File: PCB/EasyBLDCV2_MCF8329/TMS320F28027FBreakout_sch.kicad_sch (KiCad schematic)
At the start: 20 parts, among them J2 FTSH-105-01-F-DV-P-TR, U2 TMS320F28027FPTT

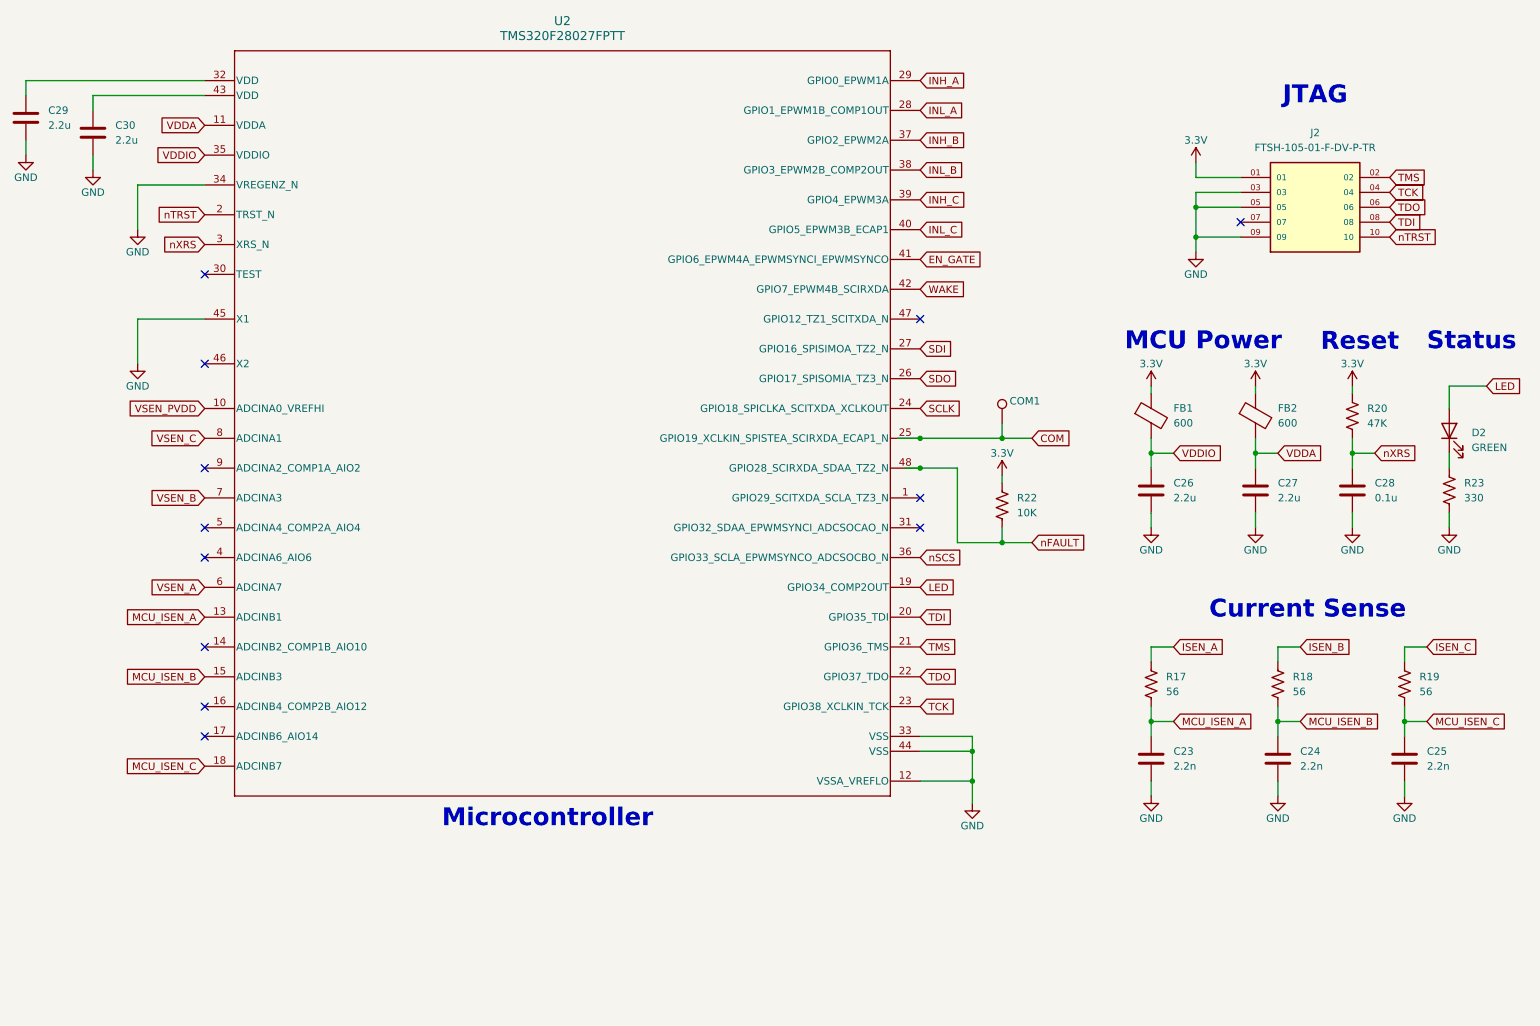
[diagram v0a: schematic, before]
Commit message: Deleted V1 Relics, redid power stage
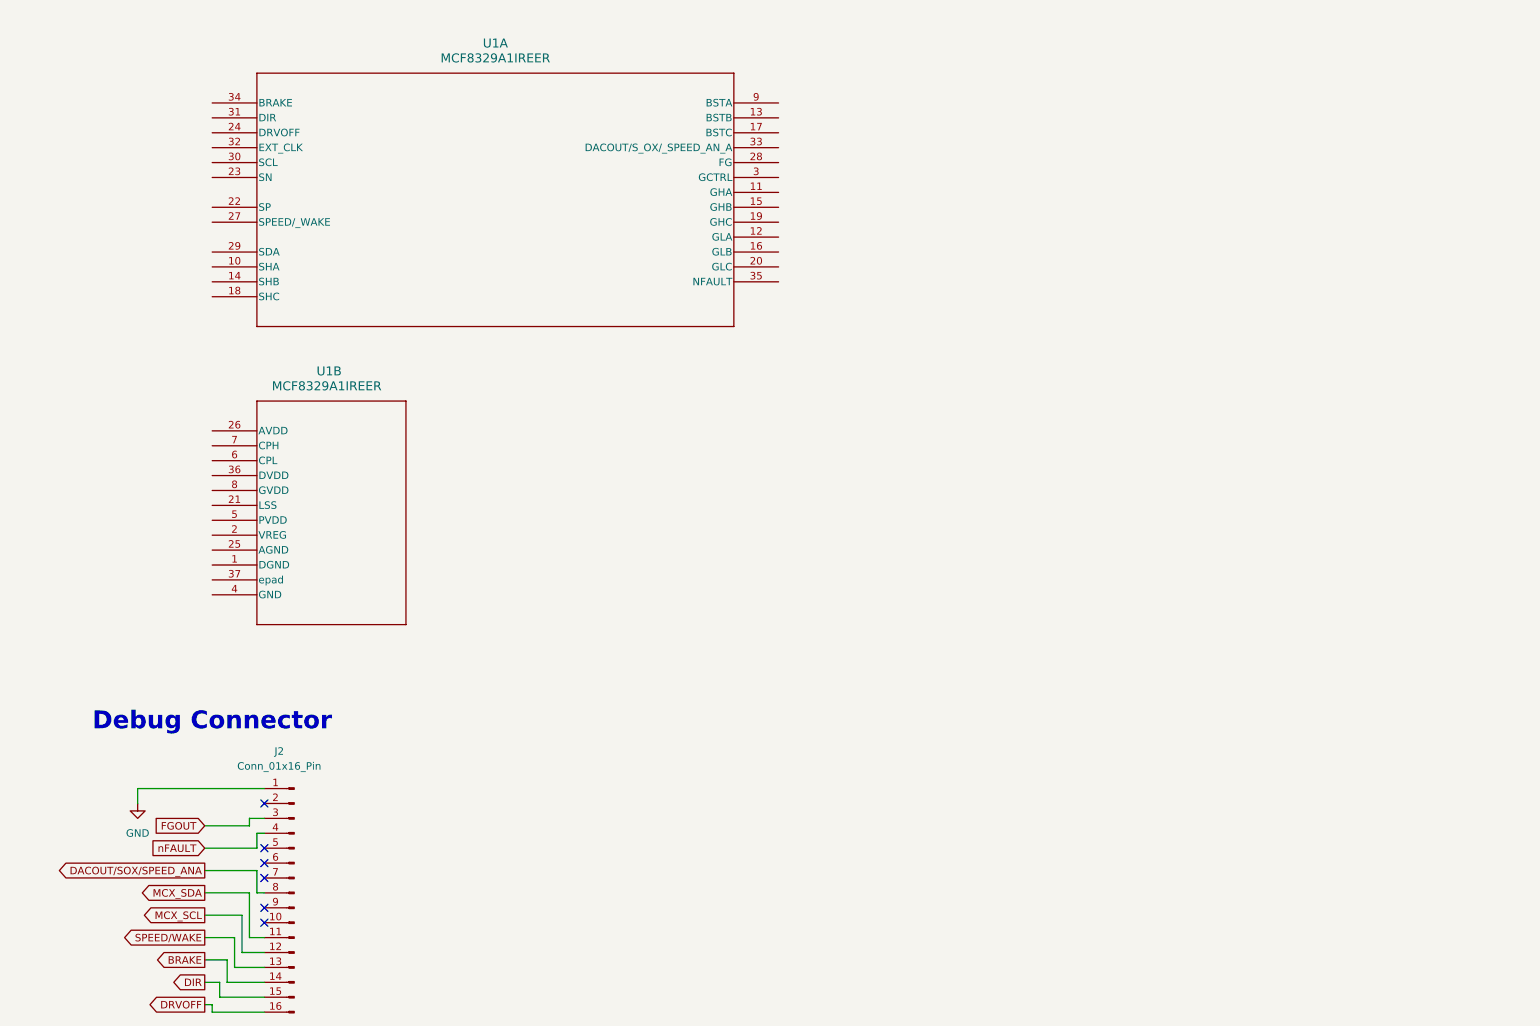
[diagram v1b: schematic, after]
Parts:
- removed C23, C24, C25: 2.2n, Capacitor_SMD:C_0402_1005Metric, symbol Device:C
- removed C26, C27, C29, C30: 2.2u, Capacitor_SMD:C_0603_1608Metric, symbol Device:C
- removed C28: 0.1u, Capacitor_SMD:C_0402_1005Metric, symbol Device:C
- removed COM1: TestPoint, TestPoint:TestPoint_Pad_D2.0mm, symbol Connector:TestPoint
- removed D2: GREEN, LED_SMD:LED_0805_2012Metric, symbol Device:LED
- removed FB1, FB2: 600, Inductor_SMD:L_0603_1608Metric, symbol Device:FerriteBead
- removed J2: FTSH-105-01-F-DV-P-TR, EasyBLDC:SAMTEC_FTSH-105-01-F-DV-P-TR, symbol EasyBLDC:FTSH-105-01-F-DV-P-TR
- removed R17, R18, R19: 56, Resistor_SMD:R_0402_1005Metric, symbol Device:R_US
- removed R20: 47K, Resistor_SMD:R_0603_1608Metric, symbol Device:R_US
- removed R22: 10K, Resistor_SMD:R_0603_1608Metric, symbol Device:R_US
- removed R23: 330, Resistor_SMD:R_0603_1608Metric, symbol Device:R_US
- removed U2: TMS320F28027FPTT, EasyBLDC:PT0048A_N, symbol EasyBLDC:TMS320F28027FPTT
- added J2: Conn_01x16_Pin, symbol Connector:Conn_01x16_Pin
- added U1: MCF8329A1IREER, WQFN36_REE_TEX, symbol EasyBLDC:MCF8329A1IREER
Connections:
- net GND: now also J2.1 (Pin_1)
- net nFAULT: now also J2.4 (Pin_4)
- new net BRAKE: J2.14 (Pin_14)
- new net DACOUT/SOX/SPEED_ANA: J2.8 (Pin_8)
- new net DIR: J2.15 (Pin_15)
- new net DRVOFF: J2.16 (Pin_16)
- new net FGOUT: J2.3 (Pin_3)
- new net MCX_SCL: J2.12 (Pin_12)
- new net MCX_SDA: J2.11 (Pin_11)
- new net SPEED/WAKE: J2.13 (Pin_13)
- no-connect marks 12 -> 6
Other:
- note added: "Debug Connector"
- note removed: "Current Sense"
- note removed: "JTAG"
- note removed: "MCU Power"
- note removed: "Microcontroller"
- note removed: "Reset"
- note removed: "Status"
- title: Easy ESC -> Easy BLDC

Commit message: Broke-out mcf8329
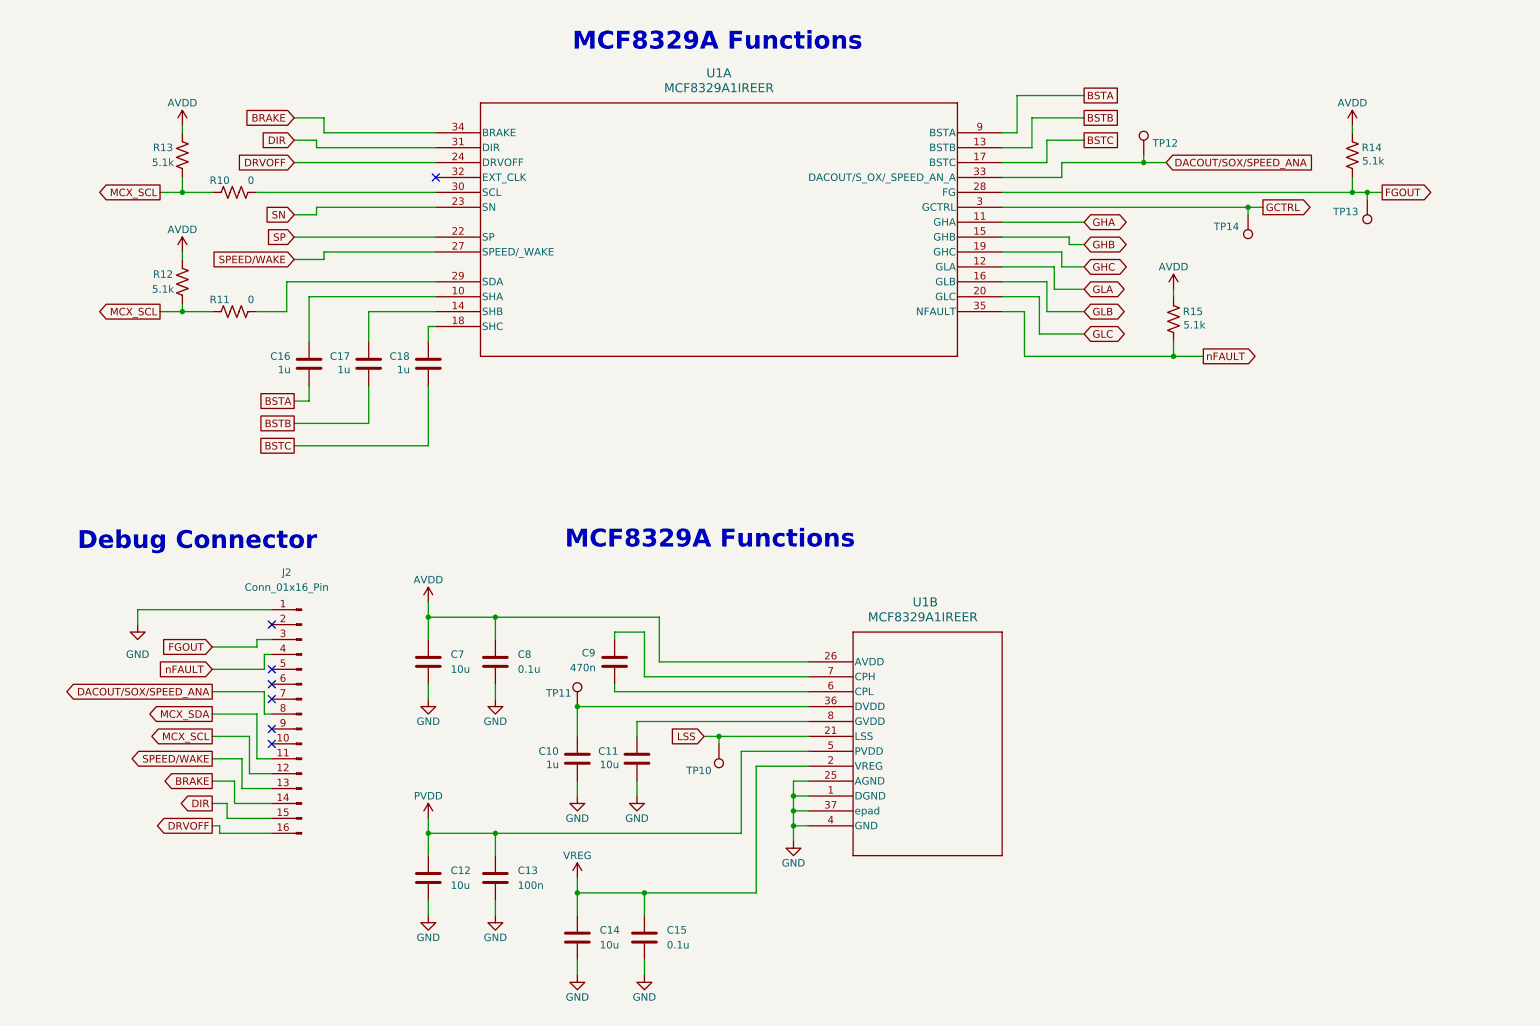
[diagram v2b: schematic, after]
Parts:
- added C10, C16, C17, C18: 1u, symbol Device:C
- added C11, C12, C14, C7: 10u, symbol Device:C
- added C13: 100n, symbol Device:C
- added C15, C8: 0.1u, symbol Device:C
- added C9: 470n, symbol Device:C
- added R10, R11: 0, Resistor_SMD:R_2512_6332Metric, symbol Device:R_US
- added R12, R13, R14, R15: 5.1k, Resistor_SMD:R_2512_6332Metric, symbol Device:R_US
- added TP10, TP11, TP12, TP13, TP14: TestPoint, symbol Connector:TestPoint
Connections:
- net BRAKE: now also U1.34 (BRAKE)
- net DACOUT/SOX/SPEED_ANA: now also U1.33 (DACOUT/S_OX/_SPEED_AN_A), TP12.1
- net DIR: now also U1.31 (DIR)
- net DRVOFF: now also U1.24 (DRVOFF)
- net FGOUT: now also U1.28 (FG), R14.1, TP13.1
- net GND: now also U1.1 (DGND), U1.25 (AGND), U1.37 (epad), U1.4 (GND), C10.2, C11.2, C12.2, C13.2, C14.2, C15.2, C7.2, C8.2
- net MCX_SCL: now also R10.1, R11.1, R12.1, R13.1
- net SPEED/WAKE: now also U1.27 (SPEED/_WAKE)
- net nFAULT: now also U1.35 (NFAULT), R15.1
- net VREG: now reaches U1.2 (VREG)
- net VREG: now also C14.1, C15.1
- net LSS: now reaches U1.21 (LSS)
- net LSS: now also TP10.1
- net AVDD: now reaches U1.26 (AVDD)
- net AVDD: now also C7.1, C8.1, R12.2, R13.2, R14.2, R15.2
- net at U1.36 (DVDD): now also C10.1, TP11.1
- net PVDD: now reaches U1.5 (PVDD)
- net PVDD: now also C12.1, C13.1
- net at U1.6 (CPL): now also C9.2
- net at U1.7 (CPH): now also C9.1
- net at U1.8 (GVDD): now also C11.1
- net at U1.10 (SHA): now also C16.1
- net GHA: now reaches U1.11 (GHA)
- net GLA: now reaches U1.12 (GLA)
- net BSTB: now reaches U1.13 (BSTB)
- net BSTB: now also C17.2
- net at U1.14 (SHB): now also C17.1
- net GHB: now reaches U1.15 (GHB)
- net GLB: now reaches U1.16 (GLB)
- net BSTC: now reaches U1.17 (BSTC)
- net BSTC: now also C18.2
- net at U1.18 (SHC): now also C18.1
- net GHC: now reaches U1.19 (GHC)
- net GLC: now reaches U1.20 (GLC)
- net SP: now reaches U1.22 (SP)
- net SN: now reaches U1.23 (SN)
- net at U1.29 (SDA): now also R11.2
- net GCTRL: now reaches U1.3 (GCTRL)
- net GCTRL: now also TP14.1
- net at U1.30 (SCL): now also R10.2
- net BSTA: now reaches U1.9 (BSTA)
- net BSTA: now also C16.2
- no-connect marks 6 -> 7
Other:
- note added: "MCF8329A Functions"
- moved on the sheet: J2, U1A, U1B

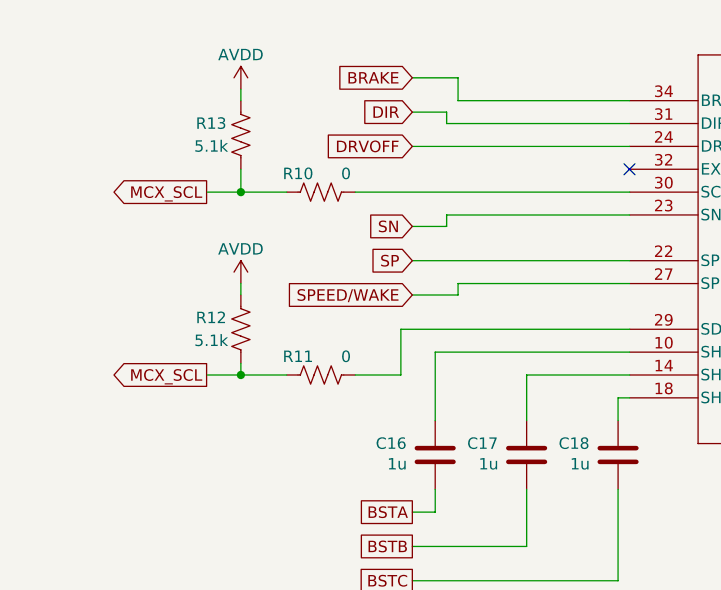
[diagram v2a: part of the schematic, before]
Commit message: Added  comments to schematic
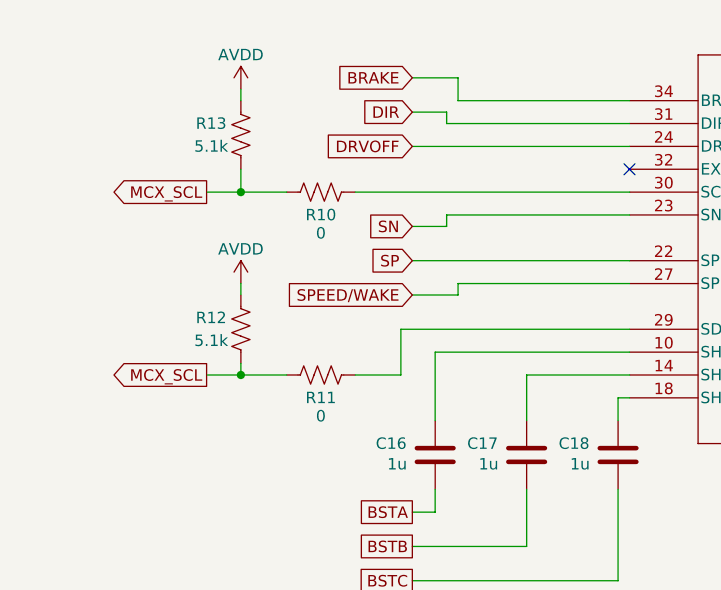
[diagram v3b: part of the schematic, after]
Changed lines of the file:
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@@
 		(dnp no)
 		(property "Reference" "R11"
-			(at 52.07 64.008 90)
+			(at 54.61 68.58 90)
 			(effects
 				(font
@@
 		)
 		(property "Value" "0"
-			(at 57.404 64.008 90)
+			(at 54.61 70.612 90)
 			(effects
 				(font
@@
 		(dnp no)
 		(property "Reference" "R10"
-			(at 52.07 43.688 90)
+			(at 54.61 48.26 90)
 			(effects
 				(font
@@
 		)
 		(property "Value" "0"
-			(at 57.404 43.688 90)
-			(effects
-				(font
+			(at 54.61 50.292 90)
+			(effects
+				(font

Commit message: Finished schematic
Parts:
- removed C14: 10u, symbol Device:C
- removed C15: 0.1u, symbol Device:C
- removed J2: Conn_01x16_Pin, symbol Connector:Conn_01x16_Pin
- added D1, D2: GREEN, symbol Device:LED
- added D3: RED, symbol Device:LED
- added R19, R21: 890, symbol Device:R_US
- added R20: 2k, symbol Device:R_US
- added TP15: TestPoint, symbol Connector:TestPoint
- R10, R11, R12, R13, R14, R15: footprint Resistor_SMD:R_2512_6332Metric -> (none)
- U1: footprint WQFN36_REE_TEX -> EasyBLDC:WQFN36_REE_TEX
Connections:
- net VREG is gone; now on net AVDD: U1.2 (VREG)
- net AVDD: now also D1.2 (A), D3.2 (A), TP15.1
- net GND: now also R19.1, R20.1
- net PVDD: now also D2.2 (A)
- net nFAULT: now also R21.1
- new net: D2.1 (K), R20.2
- new net: D1.1 (K), R19.2
- new net: D3.1 (K), R21.2
- no-connect marks 7 -> 1
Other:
- note added: "MCF8329A"
- note added: "MCF8329A Power"
- note added: "MCF8329A Status"
- note removed: "Debug Connector"
- note removed: "MCF8329A Functions"
- moved on the sheet: C10, C11, C12, C13, C16, C17, C18, C7, C8, C9, R10, R11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
